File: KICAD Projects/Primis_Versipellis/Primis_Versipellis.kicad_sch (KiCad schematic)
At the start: 27 parts, among them J2 USB_A, J3 Conn_01x05_Pin, U1 nRF52833_QDxx, Y1 32MHz

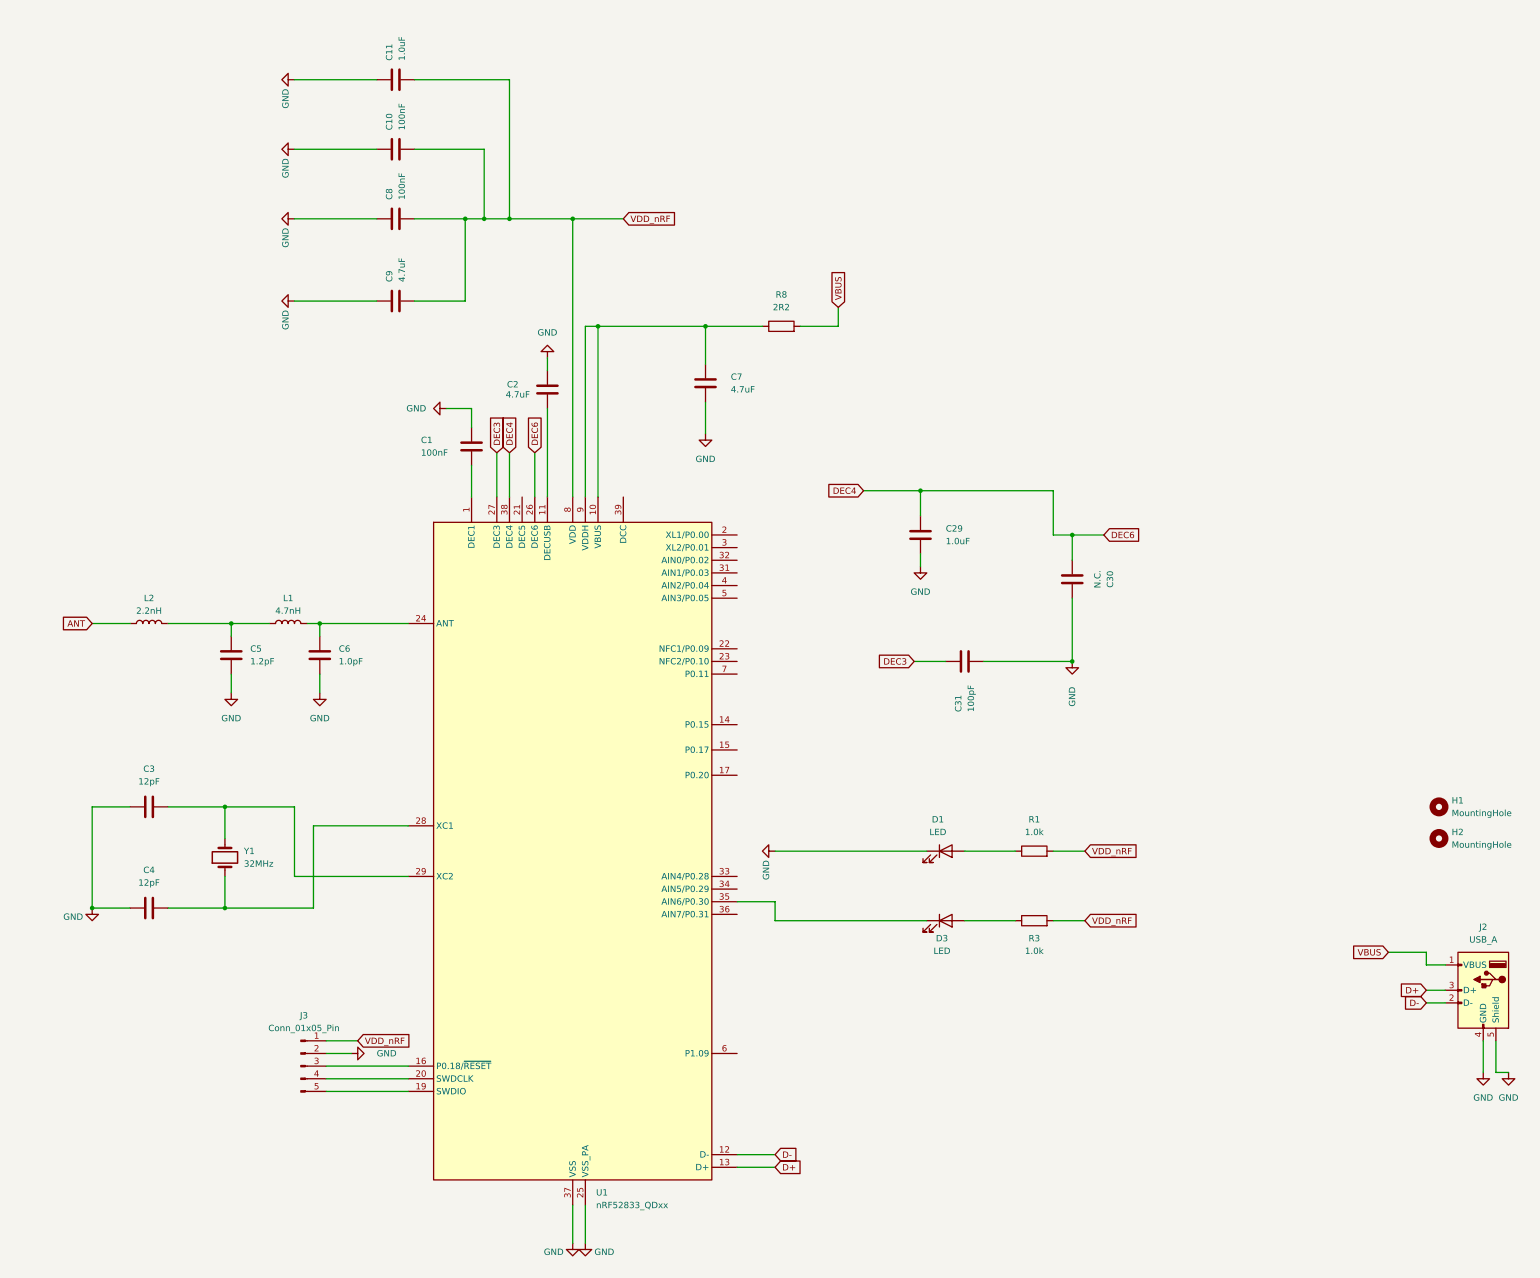
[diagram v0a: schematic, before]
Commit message: Face Tracker and Versipellis Clean
-Organised the face tracker PCB a bit more
-Added TODO to face tracker README
-Organised Versipellis schematics
-Updated images
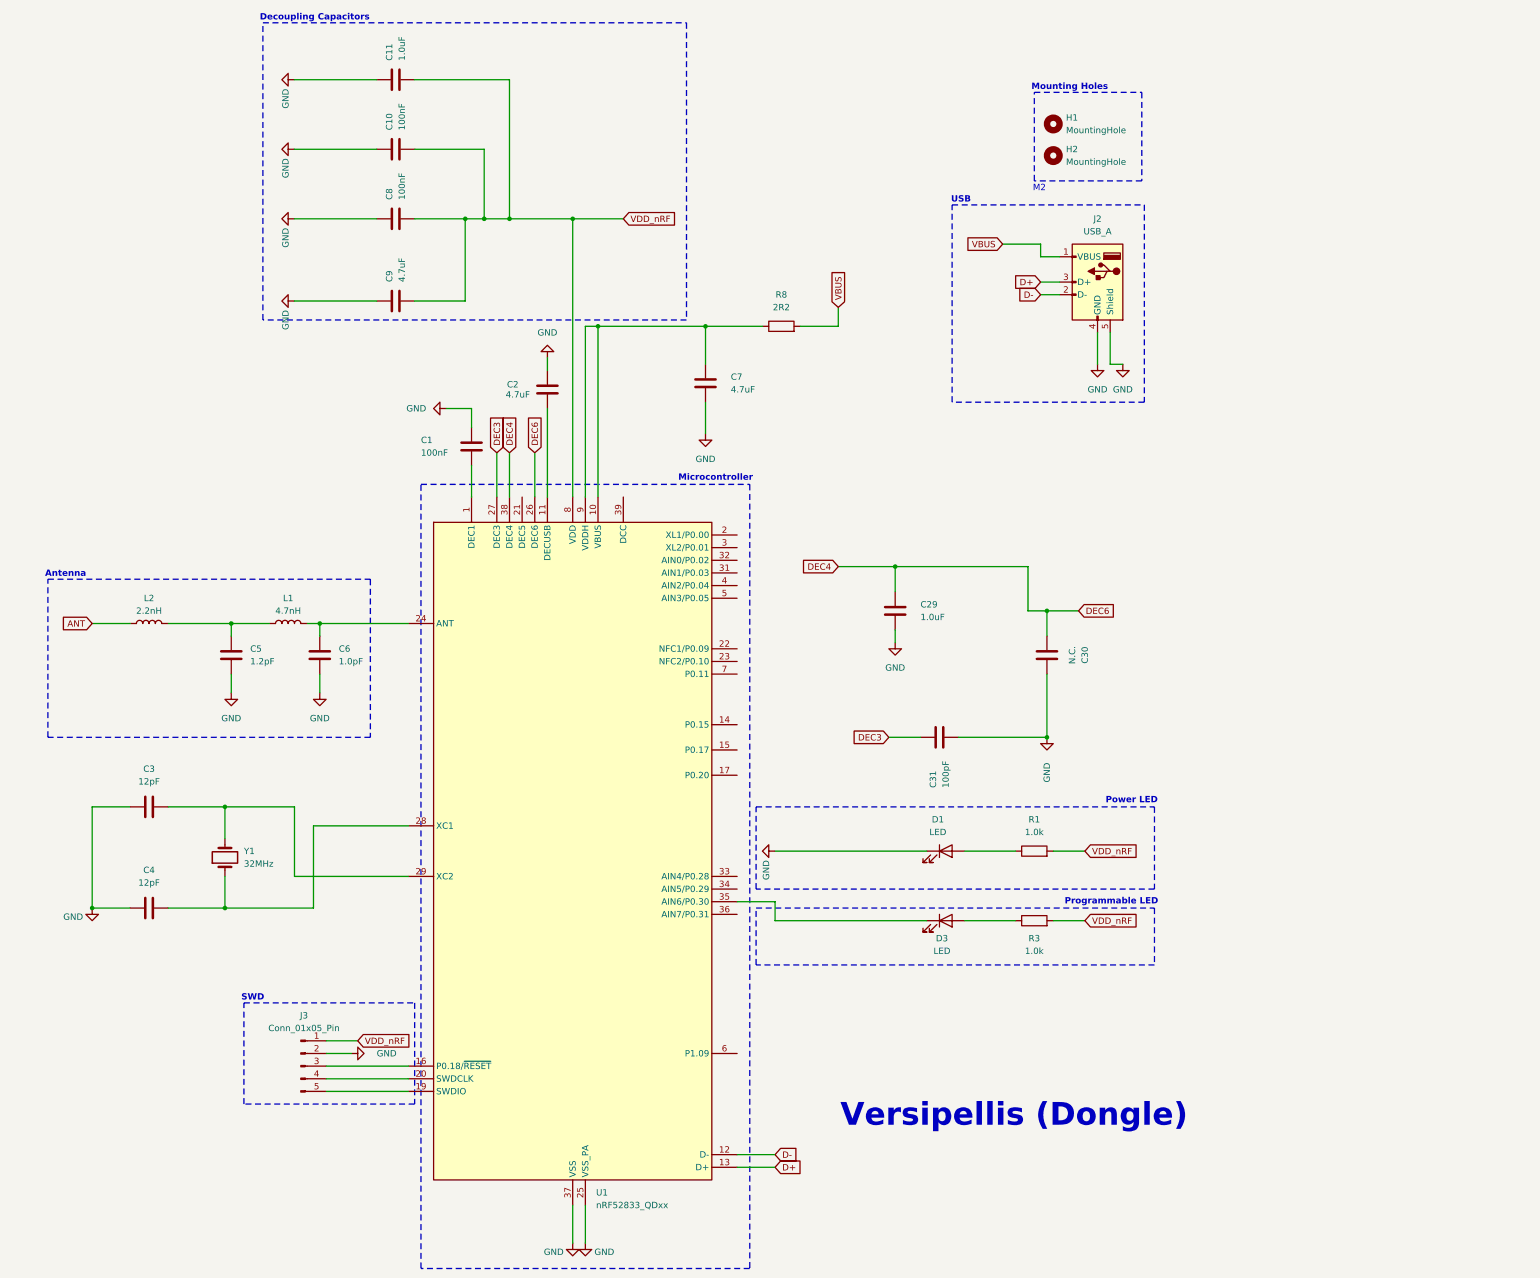
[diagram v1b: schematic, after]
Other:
- note added: "Antenna"
- note added: "Decoupling Capacitors"
- note added: "M2"
- note added: "Microcontroller"
- note added: "Mounting Holes"
- note added: "Power LED"
- note added: "Programmable LED"
- note added: "SWD"
- note added: "USB"
- note added: "Versipellis (Dongle)"
- moved on the sheet: C29, C30, C31, H1, H2, J2

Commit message: Gerbers plus clean up
-Added gerbers for the face tracker and versipellis
-Shrunk the face tracker and cleaned up
-Fixed some DRC issues with both projects
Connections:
- net DEC4 renamed DEC4_6
- no-connect marks 0 -> 18

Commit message: Quick Update
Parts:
- Y1: footprint Crystal:Crystal_SMD_5032-2Pin_5.0x3.2mm -> Crystal:Crystal_SMD_2012-2Pin_2.0x1.2mm
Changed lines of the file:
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@@
 			)
 		)
-		(property "Footprint" "Crystal:Crystal_SMD_5032-2Pin_5.0x3.2mm"
+		(property "Footprint" "Crystal:Crystal_SMD_2012-2Pin_2.0x1.2mm"
 			(at 54.61 196.85 0)
 			(effects

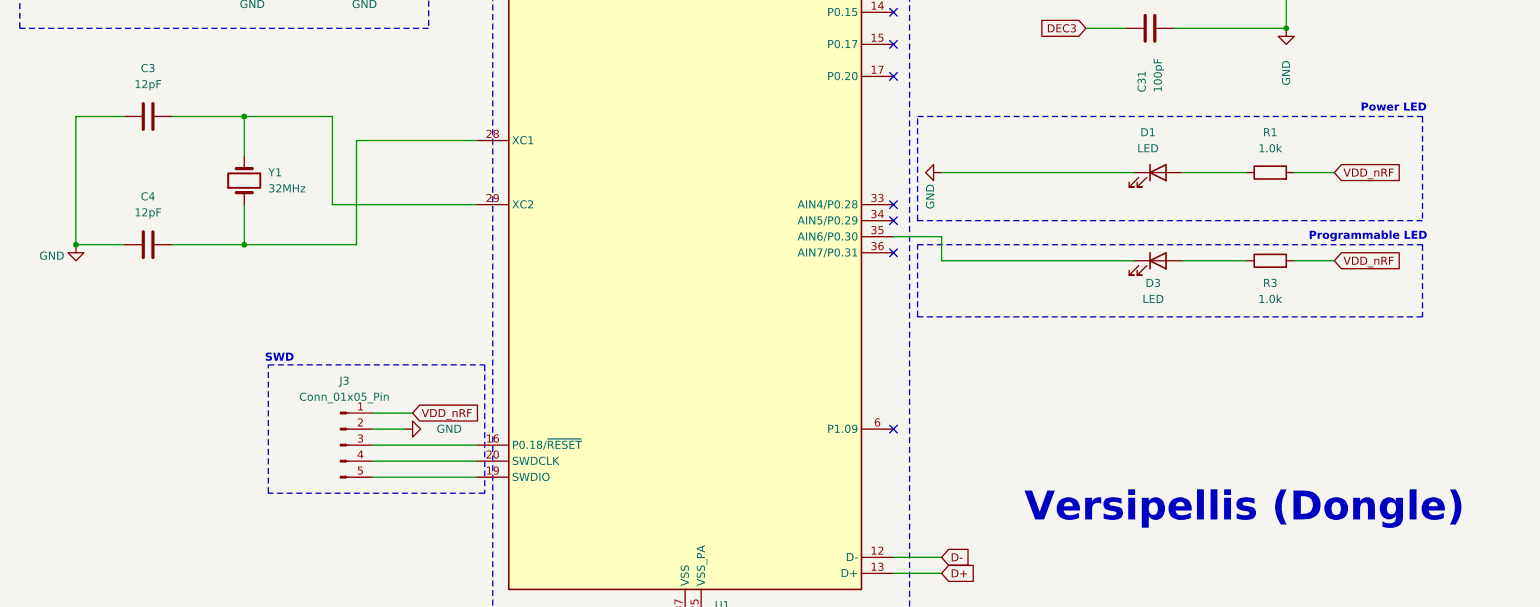
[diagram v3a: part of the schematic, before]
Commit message: FaceTracker fixes and Dongle rework
-Fixed some mistakes on the Facetracker with the camera power lines.
-Some part swaps and additions on the dongle to match the JLCPCBs catalogue
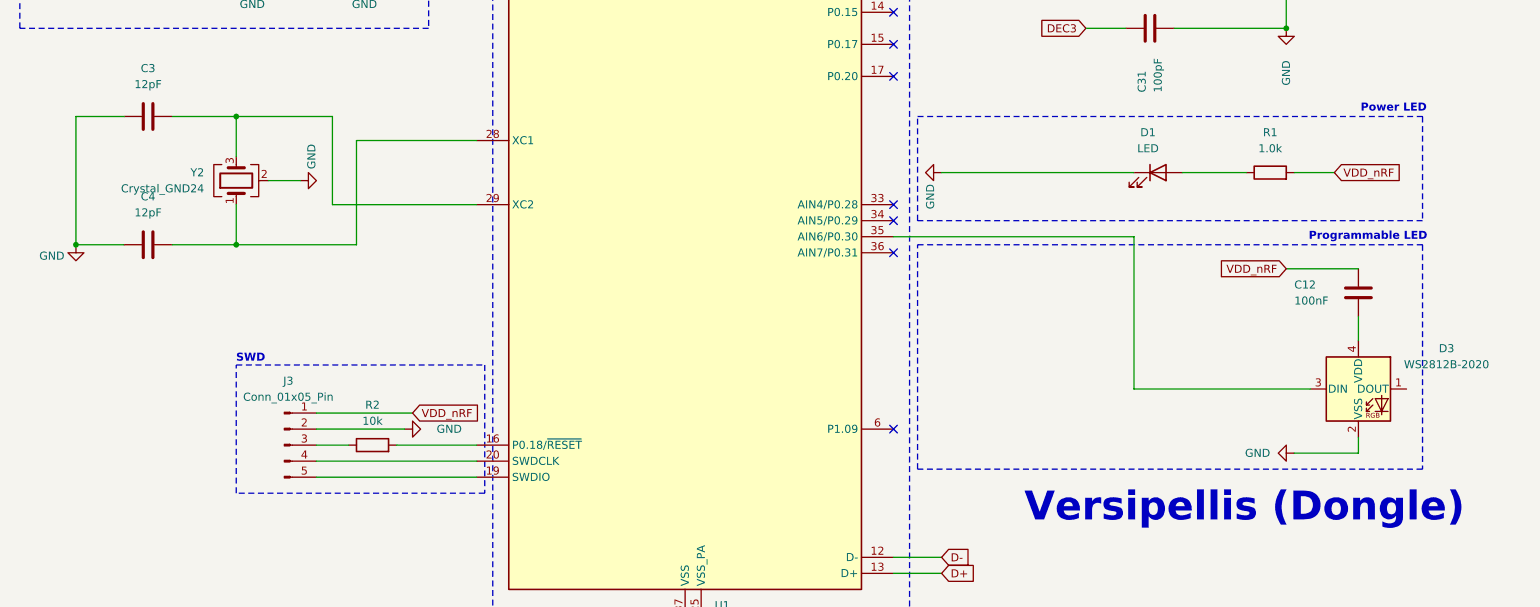
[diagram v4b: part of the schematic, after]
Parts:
- removed D3: LED, LED_SMD:LED_0603_1608Metric, symbol Device:LED
- removed R3: 1.0k, Resistor_SMD:R_0603_1608Metric, symbol Device:R
- removed Y1: 32MHz, Crystal:Crystal_SMD_2012-2Pin_2.0x1.2mm, symbol Device:Crystal
- added C12: 100nF, Capacitor_SMD:C_0603_1608Metric, symbol Device:C
- added D3: WS2812B-2020, LED_SMD:LED_WS2812B-2020_PLCC4_2.0x2.0mm, symbol LED:WS2812B-2020
- added R2: 10k, Resistor_SMD:R_0603_1608Metric, symbol Device:R
- added Y2: Crystal_GND24, Crystal:Crystal_SMD_Abracon_ABM8G-4Pin_3.2x2.5mm, symbol Device:Crystal_GND24
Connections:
- net GND: now also D3.2 (VSS), Y2.2 (G), Y2.4 (G)
- net VDD_nRF: now also C12.1
- net at U1.35 (AIN6/P0.30): now also D3.3 (DIN)
- net at J3.3 (Pin_3): now also R2.1; no longer U1.16 (P0.18/~{RESET})
- net at C4.2, U1.28 (XC1): now also Y2.1
- net at C3.2, U1.29 (XC2): now also Y2.3
- new net: R2.2, U1.16 (P0.18/~{RESET})
- new net: C12.2, D3.4 (VDD)
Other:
- moved on the sheet: J3

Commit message: Usb swap
-Changed the dongle to another usb
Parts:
- J2: footprint Connector_USB:USB_A_CNCTech_1001-011-01101_Horizontal -> USB:USB05
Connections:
- no-connect marks 18 -> 19
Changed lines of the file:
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@@
 	)
 	(junction
+		(at 231.14 219.71)
+		(diameter 0)
+		(color 0 0 0 0)
+	)
+	(junction
 		(at 53.34 186.69)
 		(diameter 0)
@@
 	)
 	(no_connect
+		(at 238.76 229.87)
+	)
+	(no_connect
 		(at 114.3 124.46)
 	)
@@
 	(wire
 		(pts
+			(xy 231.14 219.71) (xy 231.14 222.25)
+		)
+		(stroke
+			(width 0)
+			(type default)
+		)
+	)
+	(wire
+		(pts
 			(xy 218.44 76.2) (xy 218.44 73.66)
 		)
@@
 	(wire
 		(pts
-			(xy 231.14 218.44) (xy 231.14 222.25)
+			(xy 231.14 218.44) (xy 231.14 219.71)
 		)
 		(stroke
@@
 			)
 		)
-		(property "Footprint" "Connector_USB:USB_A_CNCTech_1001-011-01101_Horizontal"
+		(property "Footprint" "USB:USB05"
 			(at 226.06 82.55 0)
 			(hide yes)
@@
 					(unit 1)
 				)
+			)
+		)
+	)
+	(symbol
+		(lib_id "power:PWR_FLAG")
+		(at 231.14 219.71 270)
+		(unit 1)
+		(body_style 1)
+		(exclude_from_sim no)
+		(in_bom yes)
+		(on_board yes)
+		(in_pos_files yes)
+		(dnp no)
+		(fields_autoplaced yes)
+		(property "Reference" "#FLG05"
+			(at 233.045 219.71 0)
+			(hide yes)
+			(show_name no)
+			(do_not_autoplace no)
+			(effects
+				(font
+					(size 1.27 1.27)
+				)
+			)
+		)
+		(property "Value" "PWR_FLAG"
+			(at 234.95 219.7099 90)
+			(show_name no)
+			(do_not_autoplace no)
+			(effects
+				(font
+					(size 1.27 1.27)
+				)
+				(justify left)
+			)
+		)
+		(property "Footprint" ""
+			(at 231.14 219.71 0)
+			(hide yes)
+			(show_name no)
+			(do_not_autoplace no)
+			(effects
+				(font
+					(size 1.27 1.27)
+				)
+			)
+		)
+		(property "Datasheet" ""
+			(at 231.14 219.71 0)
+			(hide yes)
+			(show_name no)
+			(do_not_autoplace no)
+			(effects
+				(font
+					(size 1.27 1.27)
+				)
+			)
+		)
+		(property "Description" "Special symbol for telling ERC where power comes from"
+			(at 231.14 219.71 0)
+			(hide yes)
+			(show_name no)
+			(do_not_autoplace no)
+			(effects
+				(font
+					(size 1.27 1.27)
+				)
+			)
+		)
+		(pin "1"
+		)
+		(instances
+			(project "Primis_Versipellis"
+				(path "/bae96686-1706-45b6-9136-3a0b4f8a04e3"
+					(reference "#FLG05")
+					(unit 1)
+				)

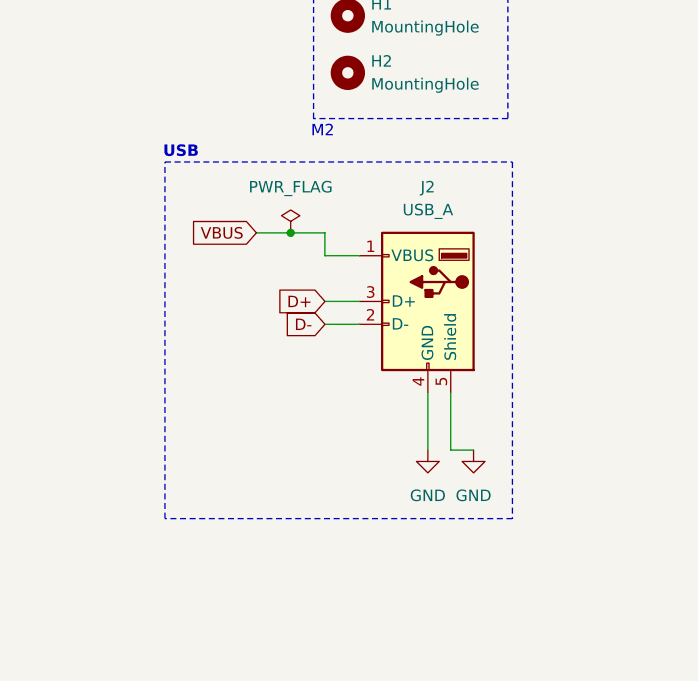
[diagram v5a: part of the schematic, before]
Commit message: Versipellis EV1 Final + General Github updates
-Fixed a few remaining issues with Versipellis EV1
-Created production files for Versipellis
-Updated pictures for all projects
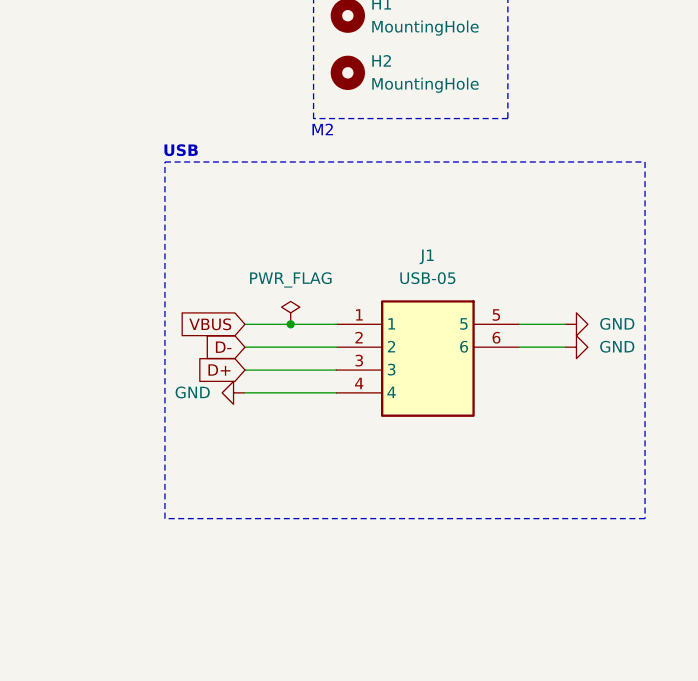
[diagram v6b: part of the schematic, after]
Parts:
- removed J2: USB_A, USB:USB05, symbol Connector:USB_A
- added J1: USB-05, Veri:USB05, symbol USB-05:USB-05
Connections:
- net D+: now also J1.3
- net D-: now also J1.2
- net GND: now also J1.4, J1.5, J1.6
- net VBUS: now also J1.1

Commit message: Quick EV1 Dongle Fixes
-Made some last minute fixes
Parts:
- J3: footprint Connector_PinHeader_1.00mm:PinHeader_1x05_P1.00mm_Vertical -> Connector_PinHeader_1.27mm:PinHeader_1x05_P1.27mm_Vertical
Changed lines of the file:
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@@
 			)
 		)
-		(property "Footprint" "Connector_PinHeader_1.00mm:PinHeader_1x05_P1.00mm_Vertical"
+		(property "Footprint" "Connector_PinHeader_1.27mm:PinHeader_1x05_P1.27mm_Vertical"
 			(at 60.96 238.76 0)
 			(hide yes)
